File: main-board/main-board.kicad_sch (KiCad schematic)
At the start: 48 parts, among them IC13 TPS2121RUXR, J1 Conn_01x08, J12 Conn_01x01_Socket, J2 Conn_01x08, J4 Conn_01x08, J47 Barrel Jack, J5 Conn_01x08, J66 Conn_01x01_Socket, J70 Conn_01x07, J72 Conn_01x07, J73 Conn_01x03, J8 Conn_01x16, P2 USB Micro, SW1 SW_SPDT, SW2 SW_SPDT, SW3 SW_SPDT, SW5 SW_Push, U3 TLV75801PDBV

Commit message: Finished ADC/DAC board
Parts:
- added C97: 0.1u, Capacitor_SMD:C_0603_1608Metric, symbol Device:C_Small
- added CG1, CG10, CG11, CG12, CG2, CG3, CG4, CG5, CG6, CG7, CG8, CG9: ~, heep_footprints:chewing-gum, symbol cheeps-tb:chewing-gum
- added J20: Conn_01x01_Pin, Connector_PinHeader_2.54mm:PinHeader_1x01_P2.54mm_Vertical, symbol Connector:Conn_01x01_Pin
- added U25: TCA9554ADBQR, Package_SO:SSOP-16_3.9x4.9mm_P0.635mm, symbol Interface_Expansion:TCA9554DBQ
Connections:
- net +3.3V: now also C97.1, U25.16 (VDD)
- net GND: now also C97.2, U25.1 (A0), U25.2 (A1), U25.3 (A2), U25.8 (GND)
- new net: J20.1 (Pin_1), U25.12 (P7)
- new net ADC_MUX: U25.11 (P6)
- new net EN_VBLADE1: U25.7 (P3)
- new net EN_VBLADE2: U25.9 (P4)
- new net EN_VBLADE3: U25.10 (P5)
- new net EN_VCGRA: U25.6 (P2)
- new net EN_VCORE: U25.5 (P1)
- new net EN_VIO: U25.4 (P0)
- new net scl: U25.15 (SDA)
- new net sda: U25.14 (SCL)
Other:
- note added: "Change this GPIO mux for the one on slack which has 16 outputs"
- note added: "I2C GPIOs"

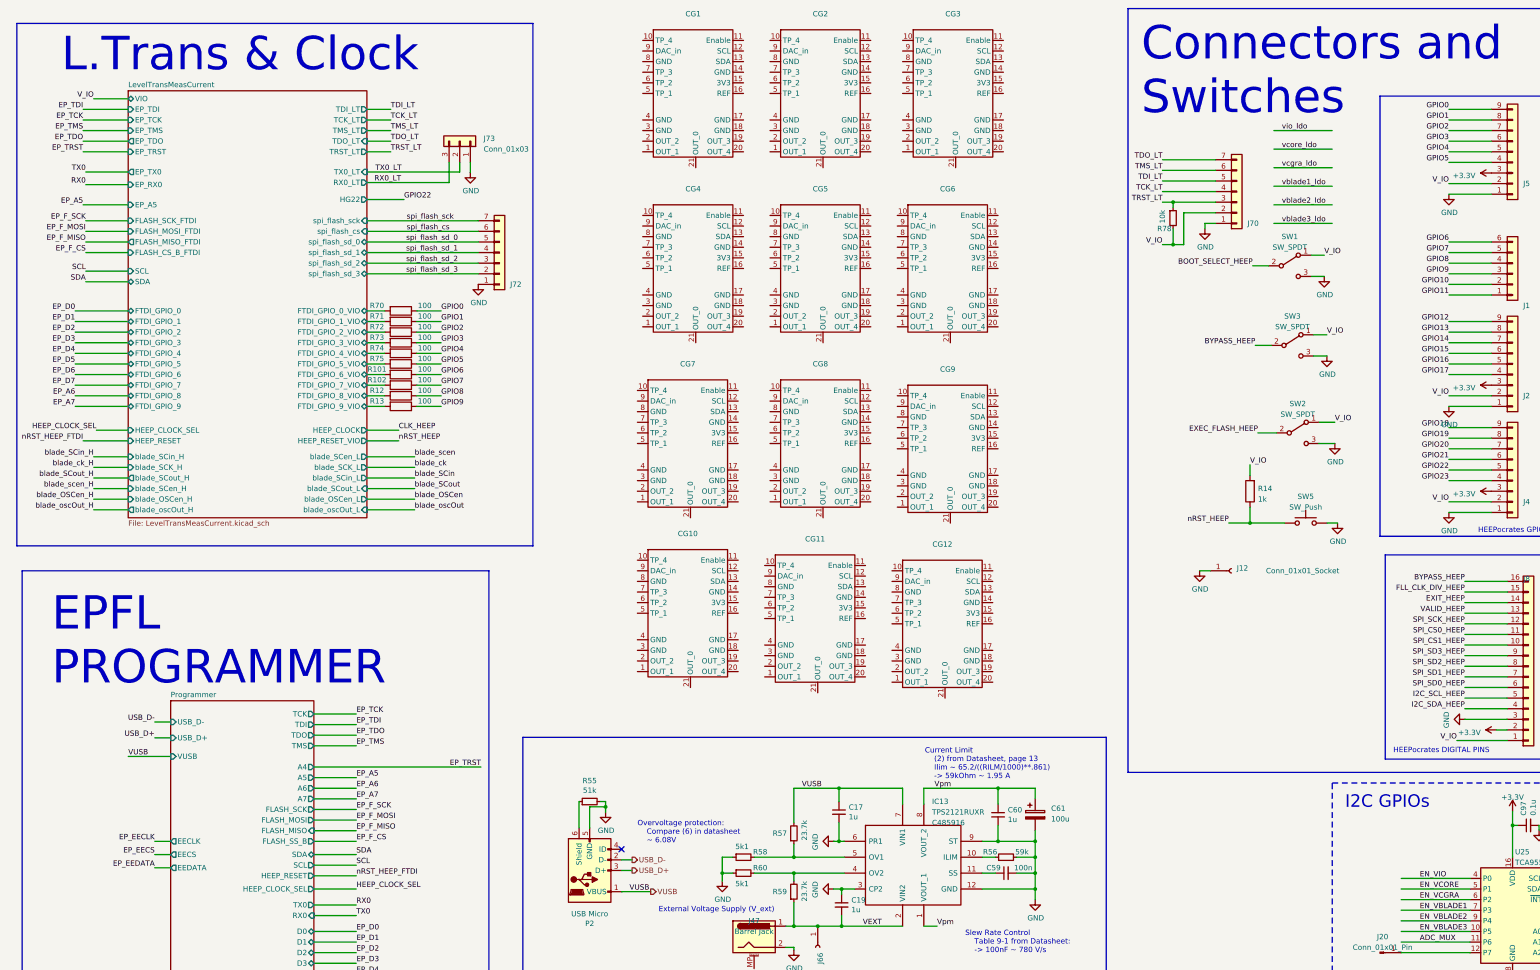
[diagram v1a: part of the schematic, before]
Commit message: re-arranged adc/dac and routed to the cgs
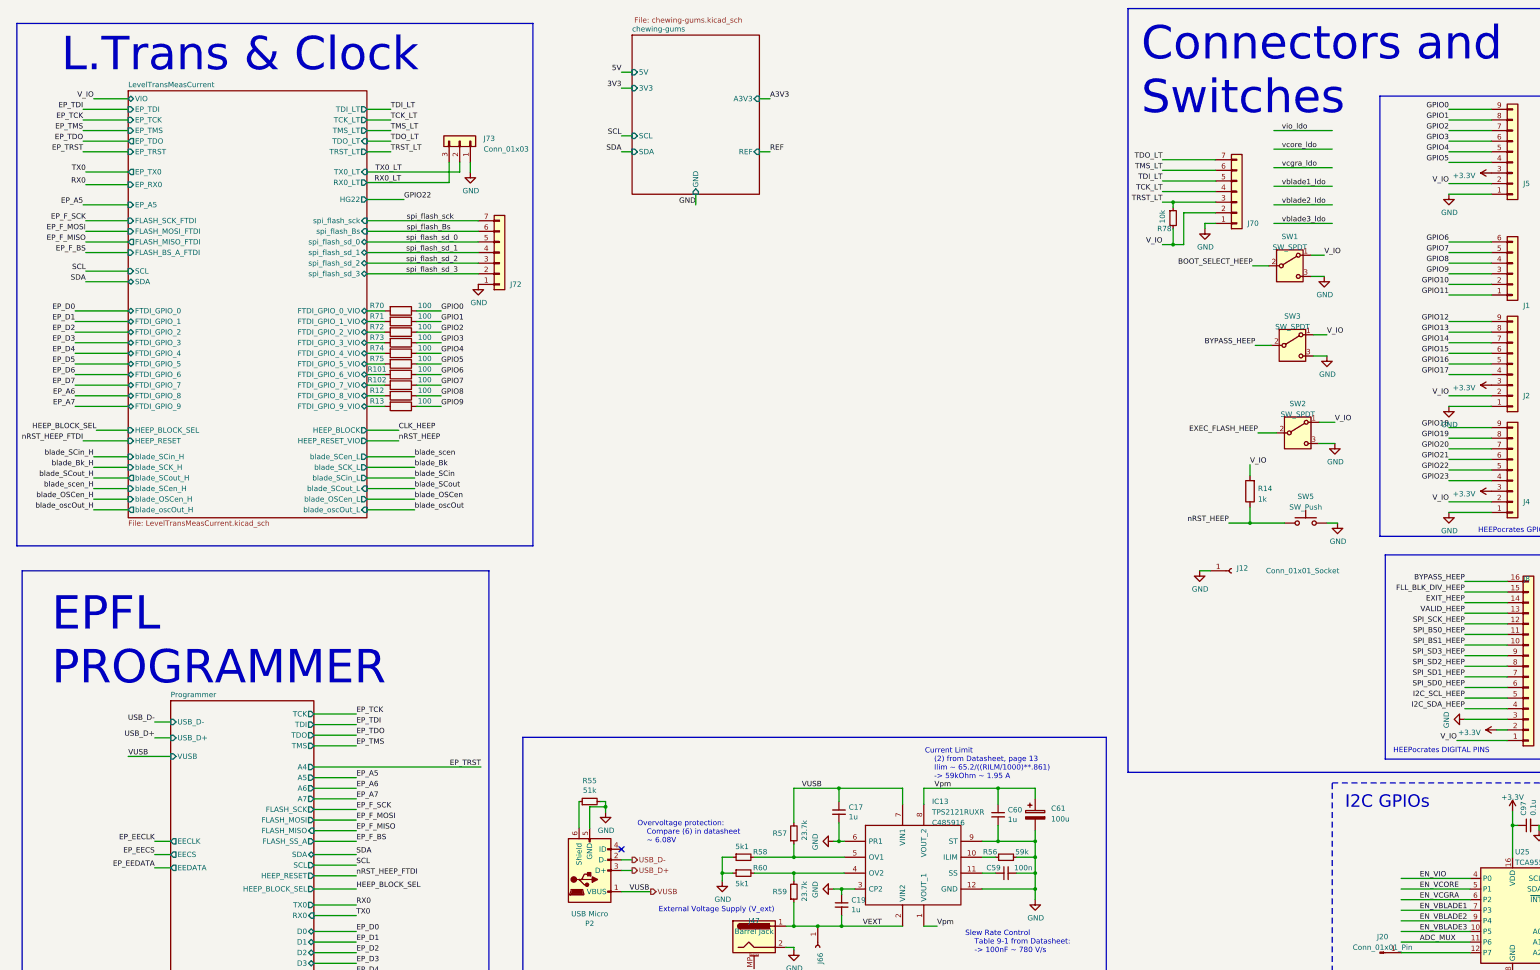
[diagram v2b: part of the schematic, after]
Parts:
- removed CG1, CG10, CG11, CG12, CG2, CG3, CG4, CG5, CG6, CG7, CG8, CG9: ~, heep_footprints:chewing-gum, symbol cheeps-tb:chewing-gum
- IC13: footprint heep_footprints:TI-VQFN-HR-12 -> SOTFL50P160X60-8N
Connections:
- net FLL_CLK_DIV_HEEP renamed FLL_BLK_DIV_HEEP
- net SPI_CS0_HEEP renamed SPI_BS0_HEEP
- net SPI_CS1_HEEP renamed SPI_BS1_HEEP
- net spi_flash_cs renamed spi_flash_Bs
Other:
- added sheet chewing-gums (chewing-gums.kicad_sch)
- sheet LevelTransMeasCurrent ports: added FLASH_BS_A_FTDI, HEEP_BLOCK, HEEP_BLOCK_SEL, spi_flash_Bs; removed FLASH_CS_B_FTDI, HEEP_CLOCK, HEEP_CLOCK_SEL, spi_flash_cs
- sheet Programmer ports: added FLASH_SS_A, HEEP_BLOCK_SEL; removed FLASH_SS_B, HEEP_CLOCK_SEL

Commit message: Before re-organizing the main board
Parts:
- removed J1: Conn_01x08, Connector_PinSocket_2.54mm:PinSocket_1x06_P2.54mm_Vertical, symbol Connector_Generic:Conn_01x06
- removed J2, J4, J5: Conn_01x08, Connector_PinSocket_2.54mm:PinSocket_1x09_P2.54mm_Vertical, symbol Connector_Generic:Conn_01x09
- removed J70, J72: Conn_01x07, Connector_PinSocket_2.54mm:PinSocket_1x07_P2.54mm_Vertical, symbol Connector_Generic:Conn_01x07
- removed J8: Conn_01x16, Connector_PinSocket_2.54mm:PinSocket_1x16_P2.54mm_Vertical, symbol Connector_Generic:Conn_01x16
- removed R78: 10k, Resistor_SMD:R_0603_1608Metric, symbol Device:R_Small
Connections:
- net +3.3V is gone; now on net 3V3: C97.1, U25.16 (VDD)
- net 3V3_LDO is gone; now on net 3V3: C22.1, D7.2 (A), R46.2, U3.5 (OUT)
- net Vpm is gone; now on net 5V: C20.1, C60.1, C61.1, IC13.1 (VOUT_1), IC13.8 (VOUT_2), R45.2, U3.1 (IN)
- net V_IO renamed VDD_IO
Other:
- sheet chewing-gums ports: added VDD_IO; removed none
- note removed: "HEEPocrates DIGITAL PINS"
- note removed: "HEEPocrates GPIO PINS"
- moved on the sheet: C97, J12, J20, R14, SW1, SW2, SW3, SW5, U25

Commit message: Before re-routing programmer
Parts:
- removed C97: 0.1u, Capacitor_SMD:C_0603_1608Metric, symbol Device:C_Small
- removed J20: Conn_01x01_Pin, Connector_PinHeader_2.54mm:PinHeader_1x01_P2.54mm_Vertical, symbol Connector:Conn_01x01_Pin
- removed U25: TCA9554ADBQR, Package_SO:SSOP-16_3.9x4.9mm_P0.635mm, symbol Interface_Expansion:TCA9554DBQ
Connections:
- net VDD_IO renamed VDD_IO_main
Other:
- added sheet CHEEP-CONNECTOR (cheep-connector.kicad_sch)
- added sheet IO-expander (io-expander.kicad_sch)
- sheet LevelTransMeasCurrent ports: added none; removed blade_OSCen_H, blade_OSCen_L, blade_SCK_H, blade_SCK_L, blade_SCen_H, blade_SCen_L, blade_SCin_H, blade_SCin_L, blade_SCout_H, blade_SCout_L, blade_oscOut_H, blade_oscOut_L
- sheet chewing-gums ports: added A3V3_A, A3V3_B, EN_CG_[1..12], REF_A, REF_B, Vout_A_[1..12], Vout_B_[1..12], Vout_diff_[1..12]; removed 3V3, 5V, A3V3, GND, REF, VDD_IO
- note added: "CHEEP connector"
- note added: "Chewing-gums (pwr)"
- note added: "IO expanders"
- note removed: "Change this GPIO mux for the one on slack which has 16 outputs"
- note removed: "I2C GPIOs"
- moved on the sheet: C17, C19, C20, C22, C59, C60, C61, D7, IC13, J12, J47, J66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

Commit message: WIP: added i2c expanders and re-structuring i2c distributino
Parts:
- removed J12: Conn_01x01_Socket, Connector:Banana_Jack_1Pin, symbol Connector:Conn_01x01_Socket
- removed R101, R102, R12, R13, R70, R71, R72, R73, R74, R75: 100, Resistor_SMD:R_0603_1608Metric, symbol Device:R
- removed SW1, SW2, SW3: SW_SPDT, Button_Switch_SMD:SW_SPDT_PCM12, symbol Switch:SW_SPDT
- added C23, C25: 1p, Capacitor_SMD:C_0603_1608Metric, symbol Device:C_Small
- added C24, C26, C27: 0.1u, Capacitor_SMD:C_0603_1608Metric, symbol Device:C_Small
- added J6, J8: Conn_01x03, Connector_PinHeader_2.54mm:PinHeader_1x03_P2.54mm_Vertical_SMD_Pin1Right, symbol Connector_Generic:Conn_01x03
- added J7: Conn_Boaxial, Connector_Coaxial:SMA_Amphenol_901-144_Vertical, symbol Connector:Conn_Coaxial
- added R1, R12, R13: 10k, Resistor_SMD:R_0603_1608Metric, symbol Device:R_Small
- added R4, R5: 25, Resistor_SMD:R_0603_1608Metric, symbol Device:R
- added U10: SI5351A-B-GTR, Package_SO:MSOP-10-1EP_3x3mm_P0.5mm_EP1.68x1.88mm, symbol gsb_symbols:SI5351A-B-GTR
- added U15: ~, heep_footprints:BIWIN_DTS04GE_SMD, symbol cheeps-tb:SPDT-4bit-tri-state
- added X1: OK322532.768KJBA4SL, Oscillator:Oscillator_SMD_SeikoEpson_SG8002CE-4Pin_3.2x2.5mm, symbol External-lib:OK322532.768KJBA4SL
- added Y2: NX3225GA-25.000M-STD-CRG-2, Crystal:Crystal_SMD_3225-4Pin_3.2x2.5mm, symbol Device:Crystal_GND24
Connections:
- net 3V3: now also C26.2, U10.1 (VDD)
- net BYPASS_HEEP: now also U15.3
- net GND: now also C23.2, C24.2, C25.2, C26.1, C27.2, J6.1 (Pin_1), J7.2 (Ext), U10.8 (GND), U15.6 (-), X1.2 (GND), Y2.2, Y2.4
- net VDD_IO_main: now also C24.1, C27.1, R1.1, R12.1, R13.1, U10.7 (VDDO), U15.5 (+), X1.4 (Vcc)
- net RX0_LT renamed UART.RX
- net TX0_LT renamed UART.TX
- net nRST_HEEP renamed nRST
- new net: C23.1, U10.3 (XB), Y2.1
- new net: C25.1, U10.2 (XA), Y2.3
- new net: J8.3 (Pin_3), R4.1
- new net: R4.2, U10.6 (CLK2)
- new net: J6.2 (Pin_2), R1.2, X1.1 (TRI)
- new net: J8.1 (Pin_1), R5.1
- new net: R5.2, X1.3 (OUT)
- new net BOOT_SEL: U15.1
- new net CHEEP_I2C.SCL: R13.2
- new net CHEEP_I2C.SDA: R12.2
- new net CLOCK: J7.1 (In), J8.2 (Pin_2)
- new net CLOCK_SEL: J6.3 (Pin_3)
- new net EXEC_FLASH: U15.2
- new net SCL_LEFT: U10.4 (SCL)
- new net SDA_LEFT: U10.5 (SDA)
- no-connect marks 1 -> 2
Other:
- added sheet GPIO_playground (gpio_playground.kicad_sch)
- added sheet I2C_expander (i2c_expander.kicad_sch)
- sheet CHEEP-CONNECTOR ports: added BOOT_SEL, CHEEP_I2C{SCL SDA}, CLOCK, EXEC_FLASH, EXIT_VALID, EXIT_VALUE, JTAG{TDO TDI TCK TMS TRST}, UART{TX RX}, nRST; removed SCL, SDA, VDD_IO_cheep
- sheet IO-expander ports: added none; removed SCL, SDA
- sheet LevelTransMeasCurrent ports: added FLASH_CS_A_FTDI, HEEP_CLOCK_SEL, HEEP_CLOCK_SEL_VIO, spi_flash_cs; removed EP_A5, FLASH_BS_A_FTDI, FTDI_GPIO_0, FTDI_GPIO_0_VIO, FTDI_GPIO_1, FTDI_GPIO_1_VIO, FTDI_GPIO_2, FTDI_GPIO_2_VIO, FTDI_GPIO_3, FTDI_GPIO_3_VIO, FTDI_GPIO_4, FTDI_GPIO_4_VIO, FTDI_GPIO_5, FTDI_GPIO_5_VIO, FTDI_GPIO_6, FTDI_GPIO_6_VIO, FTDI_GPIO_7, FTDI_GPIO_7_VIO, FTDI_GPIO_8, FTDI_GPIO_8_VIO, FTDI_GPIO_9, FTDI_GPIO_9_VIO, HEEP_BLOCK, HEEP_BLOCK_SEL, HG22, SCL, SDA, VIO, spi_flash_Bs
- sheet Programmer ports: added FLASH_CS_A, HEEP_CLOCK_SEL, TRST; removed A4, A5, A6, A7, D0, D1, D2, D3, D4, D5, D6, D7, FLASH_SS_A, HEEP_BLOCK_SEL
- sheet chewing-gums ports: added ADCDAC_I2C_SCL_LEFT, ADCDAC_I2C_SCL_RIGHT, ADCDAC_I2C_SDA_LEFT, ADCDAC_I2C_SDA_RIGHT, CG_I2C_SCL_[1..12], CG_I2C_SDA_[1..12]; removed SCL, SDA
- note added: "3V3"
- note added: "ADC/DAC"
- note added: "Add pushbuttons and switches connected to GPIOs on the cheep connector"
- note added: "Boot Switches"
- note added: "CG_SDA_x/CG_SCL_x / ADC_DAC_SDA_LEFT"
- note added: "CHEEP_I2C.SDA CHEEP_I2C.SCL"
- note added: "Check supply voltages are right (3V3, VDD IO main or VDD IO cheep)"
- note added: "Chewing gum"
- note added: "Chewingums"
- note added: "Clock"
- note added: "EPFL PRGM"
- note added: "Enables"
- note added: "FTDI"
- note added: "GPIO expander CHEEP"
- note added: "GPIO expander ENABLES"
- note added: "GPIO playground"
- note added: "GPIOs"
- note added: "HEEP bypass -> connect to CHEEP connector"
- note added: "I2C distribution"
- note added: "I2C exp LEFT"
- note added: "I2C exp RIGHT"
- note added: "I2C expander"
- note added: "I2C how to distribute?"
- note added: "Impedance matching of USB D+-"
- note added: "Increase the hole size for the bananas (this is nothing sexual, it's that the hole size for the connectors is not the right standard)"
- note added: "Level Shifters"
- note added: "OSC"
- note added: "Pull-up to VDD io"
- note added: "Remove jumper on the coaxial and just leave the resistors (both)"
- note added: "Run DRC on boards"
- note added: "SDA/SCL"
- note added: "Select the right part(color)/footprint for LEDs (GPIO playground)"
- note added: "Select the right part/footprint for Logic gates (GPIO playground) There is one we could repeat/take similar in the programmer sheet"
- note added: "The selected crystal is qualified to work with only the internal load capacitors. (see AN551.pdf) Still add the pads (just in case)..."
- note added: "ToDos:"
- note added: "USB/5V/3V3"
- note added: "What is connected to pad 11 of U10 (IC on the clock generation)"
- note added: "What to do with exit valid/value: LEDs through two mos?"
- note removed: "Chewing-gums (pwr)"
- note removed: "Connectors and Switches"
- note removed: "EPFL PROGRAMMER"
- note removed: "L.Trans & Clock"
- note removed: "USB/5V"
- moved on the sheet: C17, C19, C20, C22, C59, C60, C61, D7, IC13, J47, J66, J73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

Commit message: Routed all power signals and re-organized GPIOs
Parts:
- removed J8: Conn_01x03, Connector_PinHeader_2.54mm:PinHeader_1x03_P2.54mm_Vertical_SMD_Pin1Right, symbol Connector_Generic:Conn_01x03
- added D10, D12: LED, LED_SMD:LED_0603_1608Metric, symbol Device:LED
- added R28, R29, R30: 1k, Resistor_SMD:R_0603_1608Metric, symbol Device:R
- added SW1: SW_Push, Button_Switch_SMD:SW_Push_1P1T_NO_CK_KMR2, symbol Switch:SW_Push
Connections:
- net CLOCK: now also R4.1, R5.2
- net GND: now also D10.1 (K), D12.1 (K), SW1.2
- net UART.RX: now also J73.2 (Pin_2); no longer J73.3 (Pin_3)
- net UART.TX: now also J73.3 (Pin_3); no longer J73.2 (Pin_2)
- net VDD_IO_main: now also R30.2
- net at R5.1: now also X1.3 (OUT)
- new net: D10.2 (A), R28.2
- new net: D12.2 (A), R29.2
- new net BTN_FTDI: R30.1, SW1.1
- new net LED_FTDI_1: R28.1
- new net LED_FTDI_2: R29.1
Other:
- sheet GPIO_playground ports: added GPIO{PB_1 PB_2 PB_3 LED_R_1 LED_G_1 LED_B_1 LED_R_2 LED_G_2 SW_1 SW_2 SW_3 SW_4}; removed GPIO_[17..25], GPLED_1, GPLED_2, GPLED_3
- sheet IO-expander ports: added BTN_FTDI, GPIO_[5..17], LED_FTDI_1, LED_FTDI_2; removed 3V3, GPIO_[1..16]
- note added: "FTDI playground"
- note added: "INSERT HERE THE VDD IO MAIN REGULATOR"
- note removed: "Remove jumper on the coaxial and just leave the resistors (both)"
- moved on the sheet: R5

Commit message: rework main PCB: added USB-C, new connector symbol & footprints
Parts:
- removed P2: USB Micro, Connector_USB:USB_Micro-B_Molex-105017-0001, symbol Connector:USB_B_Micro
- removed R55: 51k, Resistor_SMD:R_0603_1608Metric, symbol Device:R_Small
- added C29: 0.1u, Capacitor_SMD:C_0603_1608Metric, symbol Device:C_Small
- added C30: 22uF, Capacitor_SMD:C_0603_1608Metric, symbol Device:C_Small
- added C39: 2.2uF, Capacitor_SMD:C_0603_1608Metric, symbol Device:C_Small
- added C40: 5.6nF, Capacitor_SMD:C_0603_1608Metric, symbol Device:C_Small
- added C41, C42: 4.7uF, Capacitor_SMD:C_0603_1608Metric, symbol Device:C_Small
- added C43: 10u, Capacitor_SMD:C_0603_1608Metric, symbol Device:C_Small
- added C44: 22u, Capacitor_SMD:C_0603_1608Metric, symbol Device:C_Small
- added D13, D14: PESD3V3U1UL, Diode_SMD:D_SOD-882, symbol Diode:PESD3V3U1UL
- added D15, D16, D17: LED, LED_SMD:LED_0603_1608Metric, symbol Device:LED
- added J8: USB_C_Receptacle_USB2.0_16P, Connector_USB:USB_C_Receptacle_GCT_USB4105-xx-A_16P_TopMnt_Horizontal, symbol Connector:USB_C_Receptacle_USB2.0_16P
- added J9: Conn_02x04_Odd_Even, symbol Connector_Generic:Conn_02x04_Odd_Even
- added L3: 10uH, symbol Device:L_Small
- added R43, R44: 5.1k, Resistor_SMD:R_0603_1608Metric, symbol Device:R_Small
- added R48: 51k, Resistor_SMD:R_0603_1608Metric, symbol Device:R_Small
- added R49: 226k, Resistor_SMD:R_0603_1608Metric, symbol Device:R_Small
- added R50: 49.9k, Resistor_SMD:R_0603_1608Metric, symbol Device:R_Small
- added R51: 3.32M, Resistor_SMD:R_0603_1608Metric, symbol Device:R_Small
- added R52: 1.33M, Resistor_SMD:R_0603_1608Metric, symbol Device:R_Small
- added R53: 10k, Resistor_SMD:R_0603_1608Metric, symbol Device:R_Small
- added R54, R55: 1.5k, Resistor_SMD:R_0603_1608Metric, symbol Device:R
- added R61: 100k, Resistor_SMD:R_0603_1608Metric, symbol Device:R_Small
- added R62, R69: 20k, Resistor_SMD:R_0603_1608Metric, symbol Device:R_Small
- added R66: 1k, Resistor_SMD:R_0603_1608Metric, symbol Device:R
- added R67: 44.2k, Resistor_SMD:R_0603_1608Metric, symbol Device:R_Small
- added R68: 86.6k, Resistor_SMD:R_0603_1608Metric, symbol Device:R_Small
- added RV1: 500k, symbol Device:R_Potentiometer
- added TP1, TP2, TP3, TP4, TP5, TP6: ~, Library:TP_50_28_RING, symbol Library:TP
- added U4: ~, symbol cheeps-tb:MAX17577
- added U5: TLV75801PDBV, Package_TO_SOT_SMD:SOT-23-5, symbol Regulator_Linear:TLV75801PDBV
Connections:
- net 3V3: now also TP3.1
- net 5V: now also C43.1, D15.2 (A), R53.2, TP2.1, U5.1 (IN)
- net GND: now also C30.1, C43.2, C44.2, D13.2 (A), D14.2 (A), J8.A1 (GND), J8.A12 (GND), J8.B1 (GND), J8.B12 (GND), L3.2, R43.2, R44.2, R48.2, R49.1, R52.2, R54.2, R55.2, R62.2, R66.2, R67.2, R68.2, R69.2, TP1.1, U5.2 (GND)
- net USB_D+: now also D13.1 (K), J8.A6 (D+), J8.B6 (D+)
- net USB_D-: now also D14.1 (K), J8.A7 (D-), J8.B7 (D-)
- net VDD_IO_main: now also C44.1, D17.2 (A), R61.2, TP6.1, U5.5 (OUT)
- net VEXT: now also TP5.1
- net VUSB: now also J8.A4 (VBUS), J8.A9 (VBUS), J8.B4 (VBUS), J8.B9 (VBUS), TP4.1
- new net: J9.5 (Pin_5), R68.1
- new net: C29.2, L3.1, U4.11 (LX)
- new net: R53.1, U5.3 (EN)
- new net: J9.2 (Pin_2), J9.4 (Pin_4), J9.6 (Pin_6), J9.8 (Pin_8), R61.1, U5.4 (FB)
- new net: R49.2, R50.1, U4.7 (FB)
- new net: J8.B5 (CC2), R44.1
- new net: C41.1, C42.1, R51.1, U4.1 (IN)
- new net: C41.2, C42.2, U4.9 (GND)
- new net: R51.2, R52.1, U4.2 (EN/UVLO)
- new net: D15.1 (K), R54.1
- new net: C29.1, U4.10 (BST)
- new net: C40.1, U4.4 (SS)
- new net: C39.1, U4.5 (VCC)
- new net: J8.A5 (CC1), R43.1
- new net: J8.S1 (SHIELD), R48.1
- new net: J9.1 (Pin_1), R62.1
- new net: J9.3 (Pin_3), R67.1
- new net: J9.7 (Pin_7), RV1.1
- new net: D16.1 (K), R55.1
- new net: R69.1, RV1.2
- new net: D17.1 (K), R66.1
- new net -5V: C30.2, C39.2, C40.2, D16.2 (A), R50.2, U4.12 (OUT), U4.8 (SOUT), U4.EP
- no-connect marks 2 -> 5
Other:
- note added: "3.3V 1.8V 1.2V ADJ (3.3V-0.655V)"
- note added: "Current Limit: (2) from Datasheet, page 13 Ilim ~ 65.2/((RILM/1000)**.861) -> 59kOhm ~ 1.95 A"
- note added: "Negative Supply"
- note added: "Slew Rate Control: Table 9-1 from Datasheet: -> 100nF ~ 780 V/s"
- note removed: "Current Limit (2) from Datasheet, page 13 Ilim ~ 65.2/((RILM/1000)**.861) -> 59kOhm ~ 1.95 A"
- note removed: "Slew Rate Control Table 9-1 from Datasheet: -> 100nF ~ 780 V/s"
- moved on the sheet: C17, C19, C20, C22, C23, C24, C25, C26, C27, C59, C60, C61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

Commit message: Connector bugfixing, added new connector to layout
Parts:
- added R70, R71: 25, Resistor_SMD:R_0603_1608Metric, symbol Device:R
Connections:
- net -5V: now also D16.1 (K); no longer D16.2 (A)
- net CLOCK: now also R71.1; no longer R4.1, R5.2
- net at R55.1: now also D16.2 (A); no longer D16.1 (K)
- net at U10.10 (CLK0): now also R71.2
- net at U10.9 (CLK1): now also R70.2
- new net CLK2: R70.1
- new net CLK3: R4.1
- new net CLK32K: R5.2
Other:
- sheet CHEEP-CONNECTOR ports: added CLOCK2, CLOCK3, CLOCK32KHZ; removed A3V3_A, A3V3_B, REF_A, REF_B
- moved on the sheet: C24, D16, J7, R1, R4, R5, U10, X1
